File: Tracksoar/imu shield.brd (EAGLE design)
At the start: 43.7 x 19.6 mm, 14 parts, among them U1 LSM9DS1, U2 HEX_CONVERTER

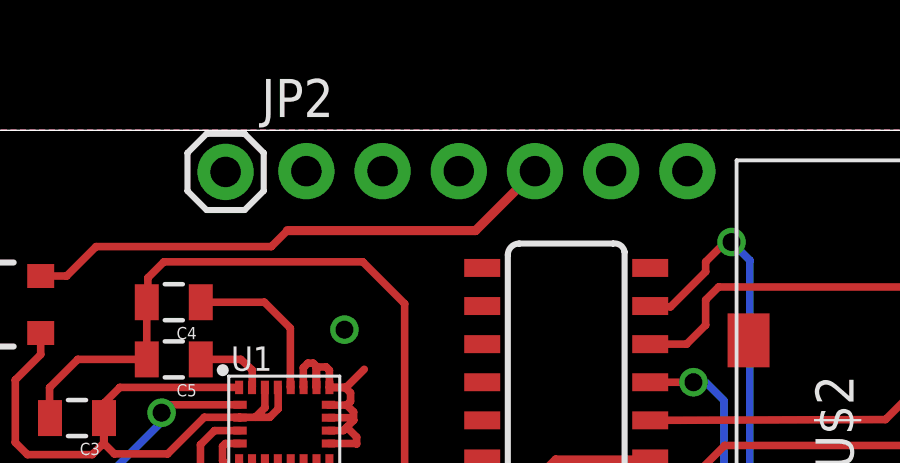
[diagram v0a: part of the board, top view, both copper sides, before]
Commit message: replace headers
replaced 2.54mm headers on all production boards with 2mm headers to
resolve daughter board issues.
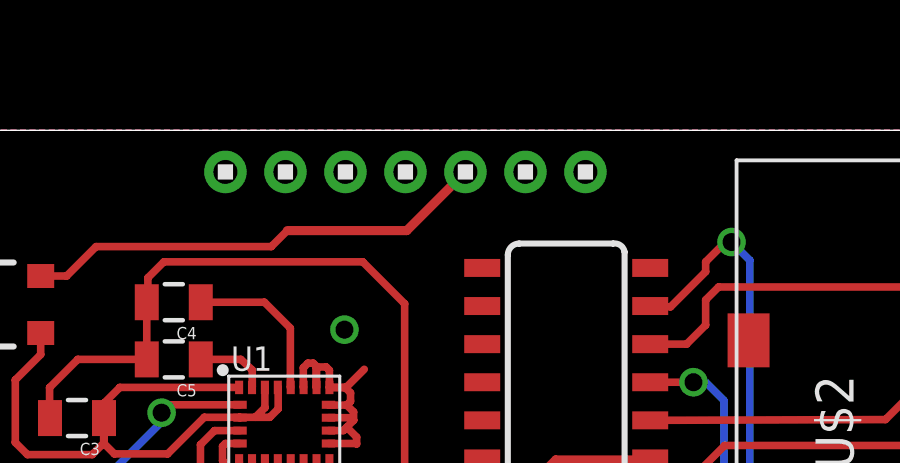
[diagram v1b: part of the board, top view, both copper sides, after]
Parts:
- removed FTDI: (no value), SparkFun-Connectors:1X06_NO_SILK
- removed JP2: (no value), SparkFun-Connectors:1X01
- added U$3: 1X7, headers(2mm):1X7
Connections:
- net !RESET: now also U$3.7; no longer JP2.1
- net DTR: now also U$3.6; no longer FTDI.1
- net GND: now also U$3.1, U$3.2; no longer FTDI.5, FTDI.6
- net RXO: now also U$3.5; no longer FTDI.2
- net TXO: now also U$3.4; no longer FTDI.3
- net VCC: now also U$3.3; no longer FTDI.4
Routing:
- net VCC: track 18.0 -> 15.6 mm
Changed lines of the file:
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@@
 </autorouter>
 <elements>
-<element name="FTDI" library="SparkFun-Connectors" package="1X06_NO_SILK" value="" x="12.9794" y="17.8562" rot="MR180">
-<attribute name="PROD_ID" value="CONN-08437" x="12.9794" y="17.8562" size="1.778" layer="28" rot="MR180" display="off"/>
-</element>
 <element name="SPI" library="SparkFun-Connectors" package="JST-4-PTH-VERT" value="" x="20.0914" y="1.651"/>
 <element name="FRAME1" library="SparkFun-Aesthetics" package="CREATIVE_COMMONS" value="FRAME-LETTER" x="14.3764" y="-8.1534"/>
 <element name="TX1" library="SparkFun-Connectors" package="JST-2-PTH-VERT" value="TX" x="14.1478" y="1.651"/>
-<element name="JP2" library="SparkFun-Connectors" package="1X01" value="" x="10.287" y="17.8308"/>
 <element name="U1" library="SparkFun-Sensors" package="LGA24-8X4" value="LSM9DS1" x="12.2428" y="9.4234">
 <attribute name="PROD_ID" value="IC-12536" x="12.2428" y="9.4234" size="1.778" layer="27" display="off"/>
@@
 </element>
 <element name="U$2" library="adafruit" package="MICROSD" value="MICROSD" x="27.2796" y="4.2164" rot="R90"/>
+<element name="U$3" library="headers(2mm)" package="1X7" value="1X7" x="16.2814" y="17.8308" rot="R180"/>
 </elements>
 <signals>
 <signal name="GND">
-<contactref element="FTDI" pad="6"/>
-<contactref element="FTDI" pad="5"/>
 <polygon width="0.4064" layer="1">
 <vertex x="-0.4064" y="19.2278"/>
@@
 <contactref element="U$2" pad="MT2"/>
 <contactref element="U2" pad="9"/>
+<contactref element="U$3" pad="1"/>
+<contactref element="U$3" pad="2"/>
 </signal>
 <signal name="VCC">
-<contactref element="FTDI" pad="4"/>
 <contactref element="U$1" pad="2"/>
 <wire x1="4.1242" y1="14.3612" x2="4.9886" y2="14.3612" width="0.254" layer="1"/>
@@
 <wire x1="5.969" y1="15.3416" x2="11.811" y2="15.3416" width="0.254" layer="1"/>
 <wire x1="11.811" y1="15.3416" x2="12.3444" y2="15.875" width="0.254" layer="1"/>
-<wire x1="20.574" y1="17.8308" x2="20.5994" y2="17.8562" width="0.254" layer="1"/>
-<wire x1="12.3444" y1="15.875" x2="18.6182" y2="15.875" width="0.3048" layer="1"/>
-<wire x1="18.6182" y1="15.875" x2="20.5994" y2="17.8562" width="0.3048" layer="1"/>
+<contactref element="U$3" pad="3"/>
+<wire x1="12.3444" y1="15.875" x2="16.3256" y2="15.875" width="0.3048" layer="1"/>
+<wire x1="16.3256" y1="15.875" x2="18.2814" y2="17.8308" width="0.3048" layer="1"/>
 </signal>
 <signal name="DTR">
-<contactref element="FTDI" pad="1"/>
+<contactref element="U$3" pad="6"/>
 </signal>
 <signal name="RXO">
-<contactref element="FTDI" pad="2"/>
+<contactref element="U$3" pad="5"/>
 </signal>
 <signal name="TXO">
-<contactref element="FTDI" pad="3"/>
+<contactref element="U$3" pad="4"/>
 </signal>
 <signal name="MISO">
@@
 </signal>
 <signal name="!RESET">
-<contactref element="JP2" pad="1"/>
+<contactref element="U$3" pad="7"/>
 </signal>
 <signal name="3V">
